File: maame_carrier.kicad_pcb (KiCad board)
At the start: 2 copper layers, 95 x 95 mm, 22 parts, among them J1 To Kakute H7 V1.5: full left 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, J10 FS-iA10B iBUS servo lead (S +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, J11 TF-Luna pin order 1-6 (CFG ti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, J12 Spare FC I2C (5 V supply, sha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, J13 Payload servo power (+ -); se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, J17 Kakute spare: T3 RSSI 3V3(FC)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, J3 VBAT tap from ESC battery pad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, J4 Micro BEC input leads (6-60 V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, J5 Micro BEC output leads (set t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, J6 Spare power: 5V_AUX G 5V_FC G, J7 Pi expansion: 3V3 logic ONLY, J8 TBS M10Q: order matches its p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, J9 SiK radio (UART4), U1 Raspberry Pi Zero W v1.1, com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

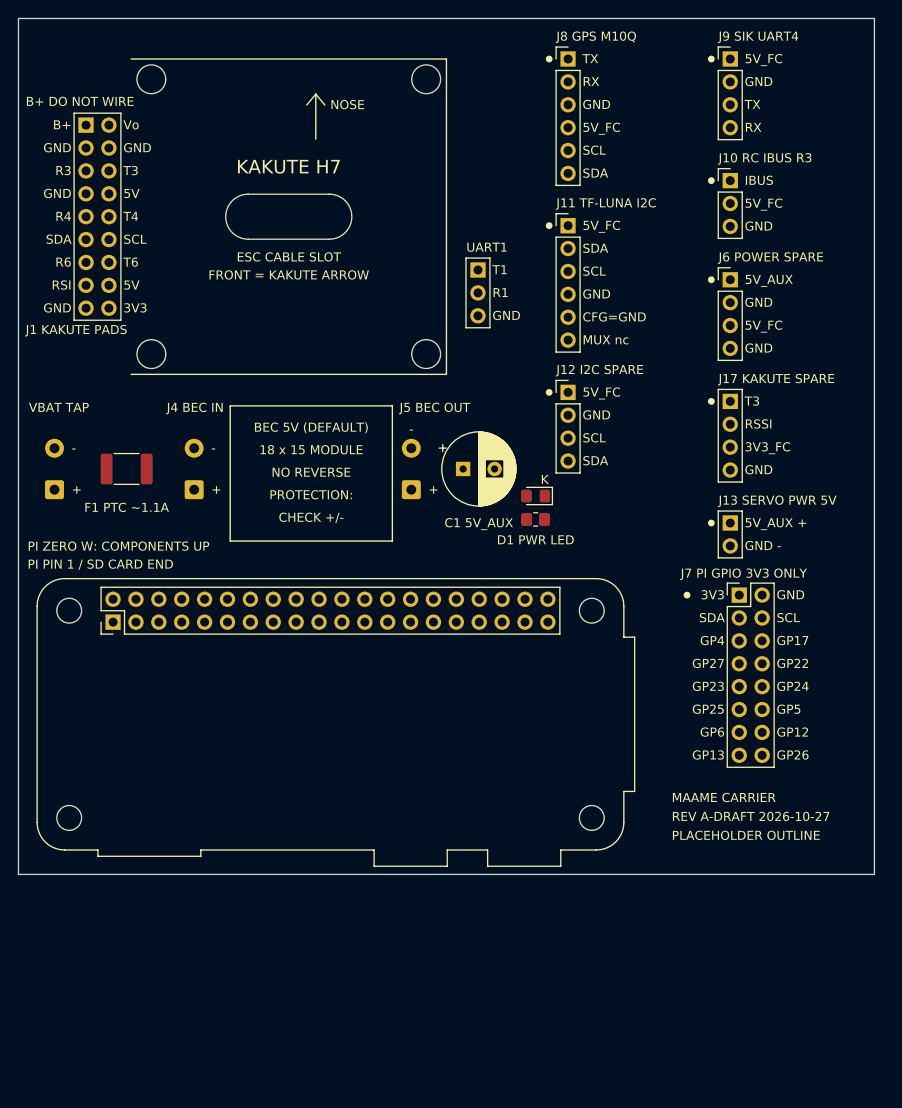
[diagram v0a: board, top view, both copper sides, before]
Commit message: J1 mirrors the Kakute's top (G 5V Vi CAM) and bottom (Z- 5V G LED) pad rows; J17 gains BUZ- and LED; J13 under J12; template and render refreshed
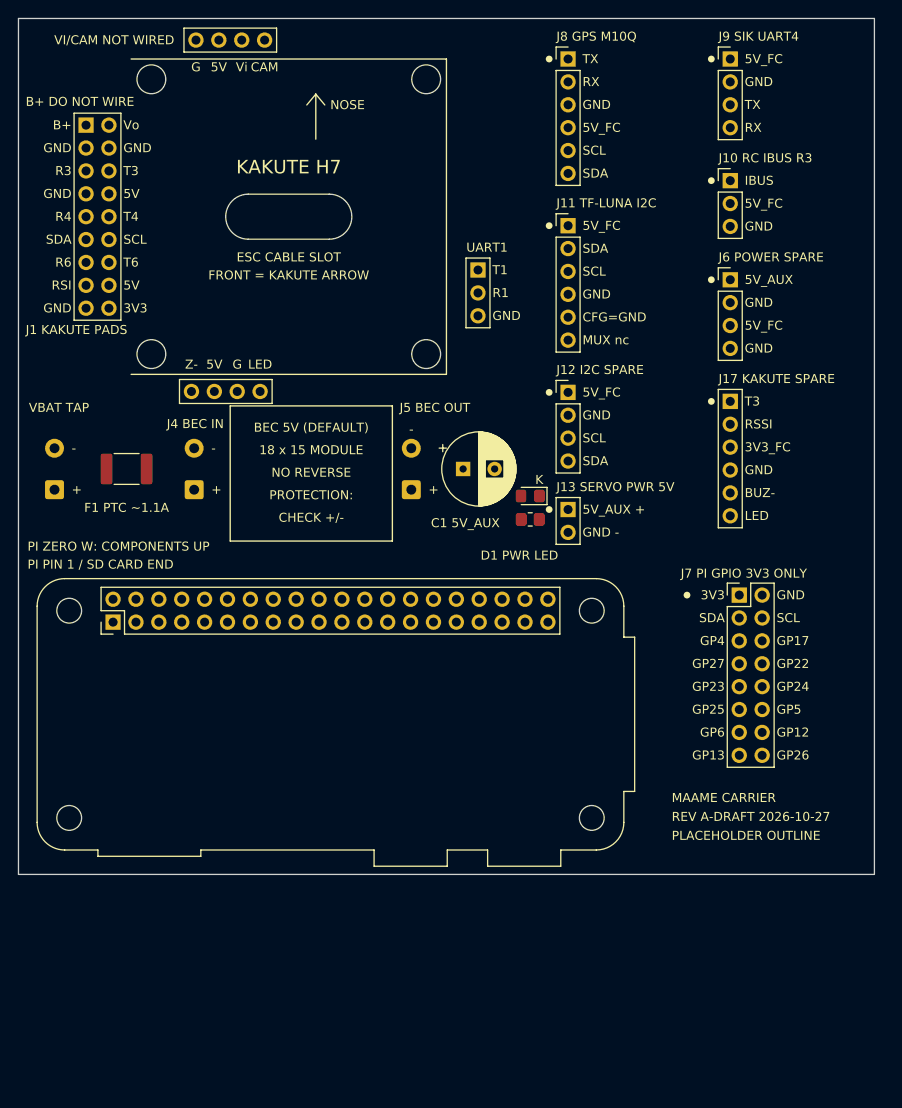
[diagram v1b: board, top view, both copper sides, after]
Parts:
- J1: value To Kakute H7 V1.5: full left pad strip 2x9 (B+ not wired) + JST T1 R1 G -> To Kakute H7 V1.5: left strip 2x9 (B+ not wired), top GND 5V Vi CAM, bottom Z- 5V GND LED, JST T1 R1 G
- J17: value Kakute spare: T3 RSSI 3V3(FC) G -> Kakute spare: T3 RSSI 3V3(FC) G BUZ- LED; footprint Connector_PinHeader_2.54mm:PinHeader_1x04_P2.54mm_Vertical -> Connector_PinHeader_2.54mm:PinHeader_1x06_P2.54mm_Vertical
- moved J13 18.1 mm to (61.0, 54.5)
- moved D1 0.60 mm to (56.8, 53.0)
- moved R1 0.60 mm to (56.8, 55.6)
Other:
- board text added: "BUZ-"
- board text added: "CAM"
- board text added: "G"
- board text added: "LED"
- board text added: "VI/CAM NOT WIRED"
- board text added: "Vi"
- board text added: "Z-"

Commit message: Frame mounting: 4x M2.5 (2.7 mm NPTH) on a 50 mm square centred on the Kakute; layout shifted, board 95x110; template updated
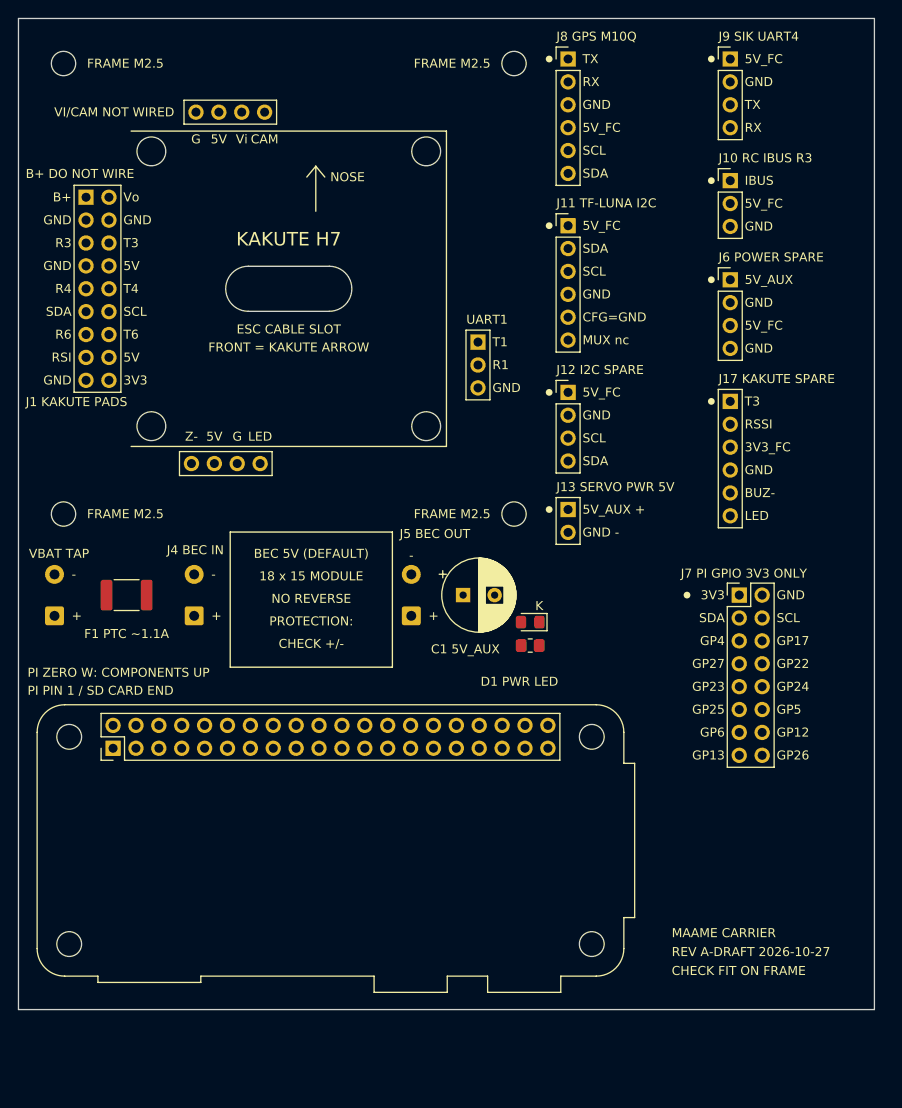
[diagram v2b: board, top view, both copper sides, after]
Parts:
- added H5: M2.5 frame mount (50 mm square), MountingHole:MountingHole_2.7mm_M2.5, F.Cu at (5.00, 5.00)
- added H6: M2.5 frame mount (50 mm square), MountingHole:MountingHole_2.7mm_M2.5, F.Cu at (55.0, 5.00)
- added H7: M2.5 frame mount (50 mm square), MountingHole:MountingHole_2.7mm_M2.5, F.Cu at (5.00, 55.0)
- added H8: M2.5 frame mount (50 mm square), MountingHole:MountingHole_2.7mm_M2.5, F.Cu at (55.0, 55.0)
- moved C1 14.0 mm to (49.4, 64.0)
- moved D1 14.0 mm to (56.8, 67.0)
- moved F1 14.0 mm to (12.0, 64.0)
- moved J3 14.0 mm to (4.00, 66.3)
- moved J4 14.0 mm to (19.5, 66.3)
- moved J5 14.0 mm to (43.6, 66.3)
- moved U1 14.0 mm to (10.5, 81.0)
- moved R1 14.0 mm to (56.8, 69.6)
- moved H1 8.00 mm to (14.8, 14.8)
- moved H2 8.00 mm to (45.2, 14.8)
- moved H3 8.00 mm to (14.8, 45.2)
- moved H4 8.00 mm to (45.2, 45.2)
- moved J1 8.00 mm to (7.50, 19.8)
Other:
- board size 95 x 95 mm -> 95 x 110 mm
- board text added: "CHECK FIT ON FRAME"
- board text added: "FRAME M2.5"
- board text removed: "PLACEHOLDER OUTLINE"

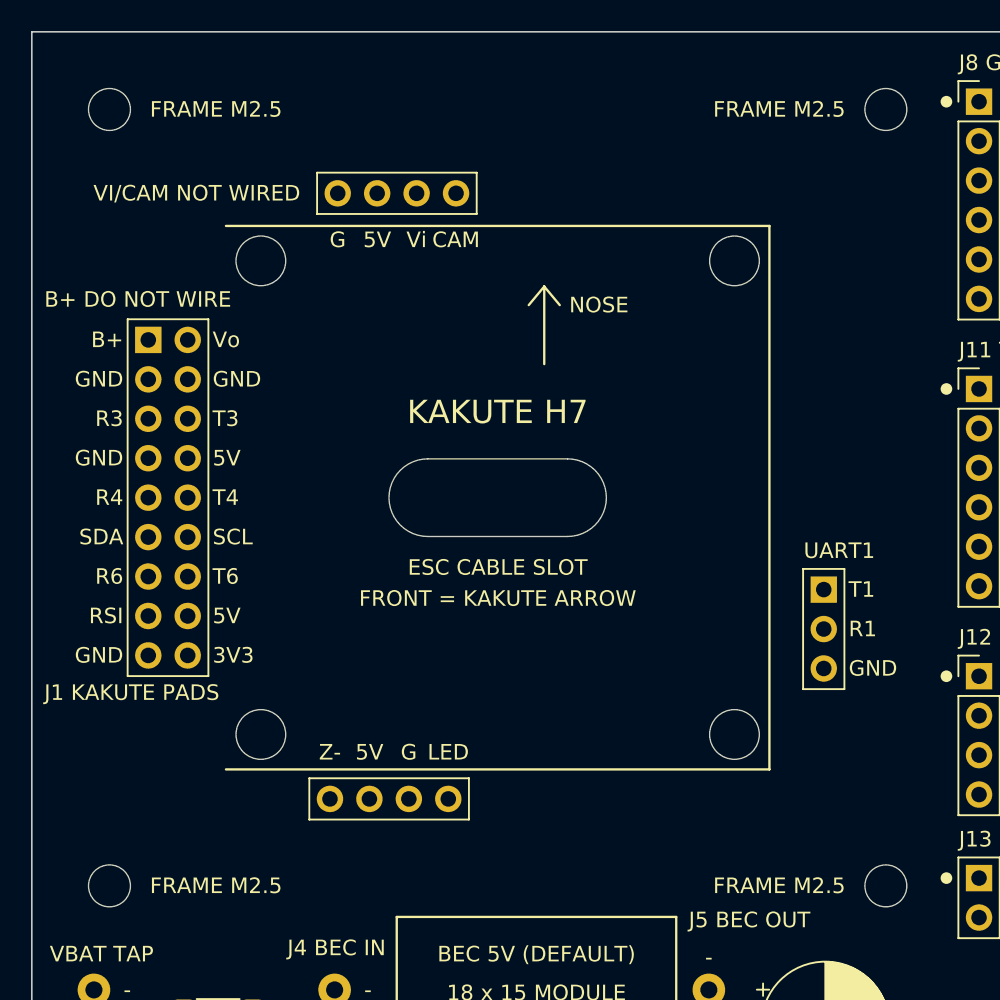
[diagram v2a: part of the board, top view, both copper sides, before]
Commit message: Frame holes measured from the pierced template: 48.3 mm square (was 50), M2.5 radial slots with +/-0.75 mm play
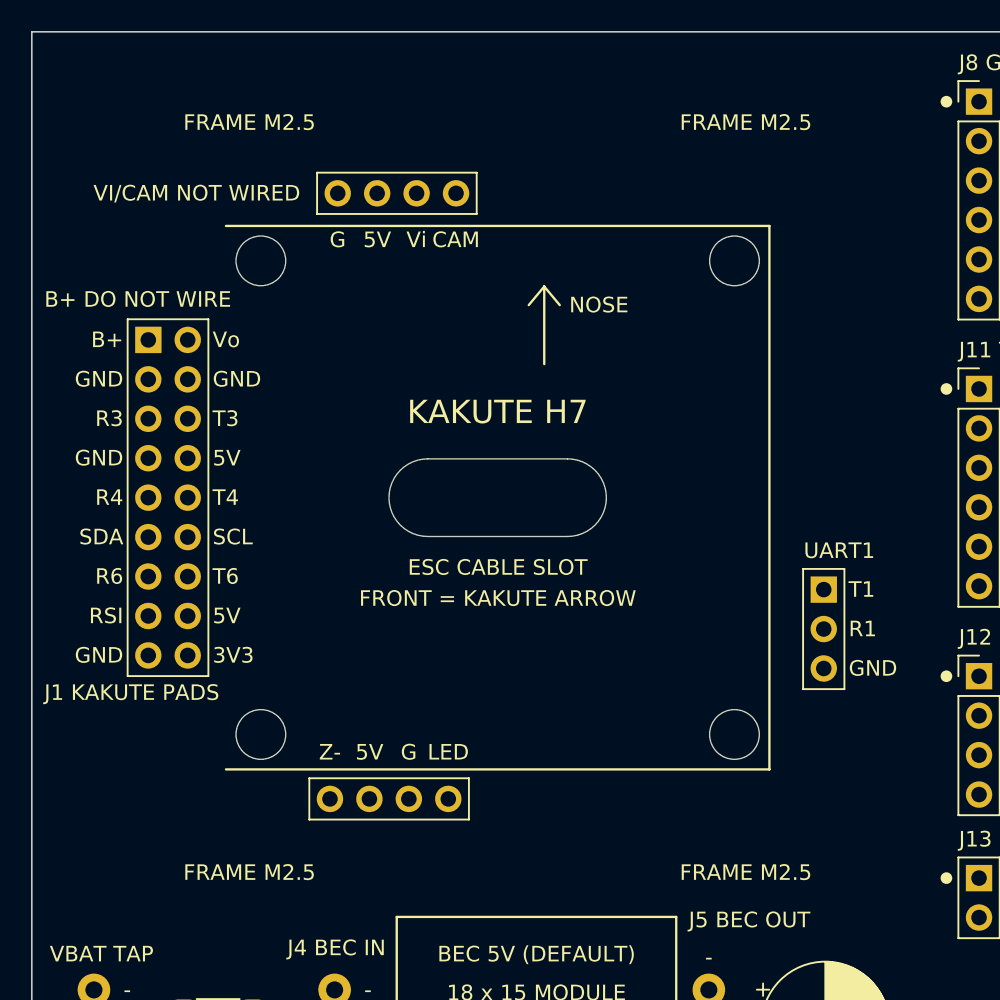
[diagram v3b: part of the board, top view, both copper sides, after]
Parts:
- H5, H6, H7, H8: value M2.5 frame mount (50 mm square) -> M2.5 frame mount, 48.3 mm square, radial slot
- moved H8 1.20 mm to (54.1, 54.1)
- moved H6 1.20 mm to (54.1, 5.85)
- moved H7 1.20 mm to (5.85, 54.1)
- moved H5 1.20 mm to (5.85, 5.85)
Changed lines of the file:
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@@
 	(footprint "MountingHole:MountingHole_2.7mm_M2.5"
 		(layer "F.Cu")
-		(at 5 5)
+		(at 5.85 5.85)
 		(descr "Mounting Hole 2.7mm, no annular, M2.5")
 		(tags "mounting hole 2.7mm no annular m2.5")
@@
 			)
 		)
-		(property "Value" "M2.5 frame mount (50 mm square)"
+		(property "Value" "M2.5 frame mount, 48.3 mm square, radial slot"
 			(at 0 3.7 0)
 			(layer "F.Fab")
@@
 		(fp_circle
 			(center 0 0)
-			(end 2.7 0)
+			(end 3.5 0)
 			(stroke
 				(width 0.15)
@@
 		(fp_circle
 			(center 0 0)
-			(end 2.95 0)
+			(end 3.7 0)
 			(stroke
 				(width 0.05)
@@
 			)
 		)
-		(pad "" np_thru_hole circle
-			(at 0 0)
-			(size 2.7 2.7)
-			(drill 2.7)
+		(pad "" np_thru_hole oval
+			(at 0 0 315)
+			(size 4.2 2.7)
+			(drill oval 4.2 2.7)
 			(layers "*.Cu" "*.Mask")
 		)
@@
 	(footprint "MountingHole:MountingHole_2.7mm_M2.5"
 		(layer "F.Cu")
-		(at 55 5)
+		(at 54.15 5.85)
 		(descr "Mounting Hole 2.7mm, no annular, M2.5")
 		(tags "mounting hole 2.7mm no annular m2.5")
@@
 			)
 		)
-		(property "Value" "M2.5 frame mount (50 mm square)"
+		(property "Value" "M2.5 frame mount, 48.3 mm square, radial slot"
 			(at 0 3.7 0)
 			(layer "F.Fab")
@@
 		(fp_circle
 			(center 0 0)
-			(end 2.7 0)
+			(end 3.5 0)
 			(stroke
 				(width 0.15)
@@
 		(fp_circle
 			(center 0 0)
-			(end 2.95 0)
+			(end 3.7 0)
 			(stroke
 				(width 0.05)
@@
 			)
 		)
-		(pad "" np_thru_hole circle
-			(at 0 0)
-			(size 2.7 2.7)
-			(drill 2.7)
+		(pad "" np_thru_hole oval
+			(at 0 0 45)
+			(size 4.2 2.7)
+			(drill oval 4.2 2.7)
 			(layers "*.Cu" "*.Mask")
 		)
@@
 	(footprint "MountingHole:MountingHole_2.7mm_M2.5"
 		(layer "F.Cu")
-		(at 5 55)
+		(at 5.85 54.15)
 		(descr "Mounting Hole 2.7mm, no annular, M2.5")
 		(tags "mounting hole 2.7mm no annular m2.5")
@@
 			)
 		)
-		(property "Value" "M2.5 frame mount (50 mm square)"
+		(property "Value" "M2.5 frame mount, 48.3 mm square, radial slot"
 			(at 0 3.7 0)
 			(layer "F.Fab")
@@
 		(fp_circle
 			(center 0 0)
-			(end 2.7 0)
+			(end 3.5 0)
 			(stroke
 				(width 0.15)
@@
 		(fp_circle
 			(center 0 0)
-			(end 2.95 0)
+			(end 3.7 0)
 			(stroke
 				(width 0.05)
@@
 			)
 		)
-		(pad "" np_thru_hole circle
-			(at 0 0)
-			(size 2.7 2.7)
-			(drill 2.7)
+		(pad "" np_thru_hole oval
+			(at 0 0 45)
+			(size 4.2 2.7)
+			(drill oval 4.2 2.7)
 			(layers "*.Cu" "*.Mask")
 		)
@@
 	(footprint "MountingHole:MountingHole_2.7mm_M2.5"
 		(layer "F.Cu")
-		(at 55 55)
+		(at 54.15 54.15)
 		(descr "Mounting Hole 2.7mm, no annular, M2.5")
 		(tags "mounting hole 2.7mm no annular m2.5")
@@
 			)
 		)
-		(property "Value" "M2.5 frame mount (50 mm square)"
+		(property "Value" "M2.5 frame mount, 48.3 mm square, radial slot"
 			(at 0 3.7 0)
 			(layer "F.Fab")
@@
 		(fp_circle
 			(center 0 0)
-			(end 2.7 0)
+			(end 3.5 0)
 			(stroke
 				(width 0.15)
@@
 		(fp_circle
 			(center 0 0)
-			(end 2.95 0)
+			(end 3.7 0)
 			(stroke
 				(width 0.05)
@@
 			)
 		)
-		(pad "" np_thru_hole circle
-			(at 0 0)
-			(size 2.7 2.7)
-			(drill 2.7)
+		(pad "" np_thru_hole oval
+			(at 0 0 315)
+			(size 4.2 2.7)
+			(drill oval 4.2 2.7)
 			(layers "*.Cu" "*.Mask")
 		)
@@
 	)
 	(gr_text "FRAME M2.5"
-		(at 7.6 5 0)
+		(at 9.75 5.85 0)
 		(layer "F.SilkS")
 		(effects
@@
 	)
 	(gr_text "FRAME M2.5"
-		(at 52.4 5 0)
+		(at 50.25 5.85 0)
 		(layer "F.SilkS")
 		(effects
@@
 	)
 	(gr_text "FRAME M2.5"
-		(at 7.6 55 0)
+		(at 9.75 54.15 0)
 		(layer "F.SilkS")
 		(effects
@@
 	)
 	(gr_text "FRAME M2.5"
-		(at 52.4 55 0)
+		(at 50.25 54.15 0)
 		(layer "F.SilkS")
 		(effects

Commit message: Frame holes to measured 48.5 mm square (M2.5 radial slots kept)
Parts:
- H5, H6, H7, H8: value M2.5 frame mount, 48.3 mm square, radial slot -> M2.5 frame mount, 48.5 mm square, radial slot
- moved H8 0.14 mm to (54.2, 54.2)
- moved H6 0.14 mm to (54.2, 5.75)
- moved H7 0.14 mm to (5.75, 54.2)
- moved H5 0.14 mm to (5.75, 5.75)
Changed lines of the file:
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@@
 	(footprint "MountingHole:MountingHole_2.7mm_M2.5"
 		(layer "F.Cu")
-		(at 5.85 5.85)
+		(at 5.75 5.75)
 		(descr "Mounting Hole 2.7mm, no annular, M2.5")
 		(tags "mounting hole 2.7mm no annular m2.5")
@@
 			)
 		)
-		(property "Value" "M2.5 frame mount, 48.3 mm square, radial slot"
+		(property "Value" "M2.5 frame mount, 48.5 mm square, radial slot"
 			(at 0 3.7 0)
 			(layer "F.Fab")
@@
 	(footprint "MountingHole:MountingHole_2.7mm_M2.5"
 		(layer "F.Cu")
-		(at 54.15 5.85)
+		(at 54.25 5.75)
 		(descr "Mounting Hole 2.7mm, no annular, M2.5")
 		(tags "mounting hole 2.7mm no annular m2.5")
@@
 			)
 		)
-		(property "Value" "M2.5 frame mount, 48.3 mm square, radial slot"
+		(property "Value" "M2.5 frame mount, 48.5 mm square, radial slot"
 			(at 0 3.7 0)
 			(layer "F.Fab")
@@
 	(footprint "MountingHole:MountingHole_2.7mm_M2.5"
 		(layer "F.Cu")
-		(at 5.85 54.15)
+		(at 5.75 54.25)
 		(descr "Mounting Hole 2.7mm, no annular, M2.5")
 		(tags "mounting hole 2.7mm no annular m2.5")
@@
 			)
 		)
-		(property "Value" "M2.5 frame mount, 48.3 mm square, radial slot"
+		(property "Value" "M2.5 frame mount, 48.5 mm square, radial slot"
 			(at 0 3.7 0)
 			(layer "F.Fab")
@@
 	(footprint "MountingHole:MountingHole_2.7mm_M2.5"
 		(layer "F.Cu")
-		(at 54.15 54.15)
+		(at 54.25 54.25)
 		(descr "Mounting Hole 2.7mm, no annular, M2.5")
 		(tags "mounting hole 2.7mm no annular m2.5")
@@
 			)
 		)
-		(property "Value" "M2.5 frame mount, 48.3 mm square, radial slot"
+		(property "Value" "M2.5 frame mount, 48.5 mm square, radial slot"
 			(at 0 3.7 0)
 			(layer "F.Fab")
@@
 	)
 	(gr_text "FRAME M2.5"
-		(at 9.75 5.85 0)
+		(at 9.65 5.75 0)
 		(layer "F.SilkS")
 		(effects
@@
 	)
 	(gr_text "FRAME M2.5"
-		(at 50.25 5.85 0)
+		(at 50.35 5.75 0)
 		(layer "F.SilkS")
 		(effects
@@
 	)
 	(gr_text "FRAME M2.5"
-		(at 9.75 54.15 0)
+		(at 9.65 54.25 0)
 		(layer "F.SilkS")
 		(effects
@@
 	)
 	(gr_text "FRAME M2.5"
-		(at 50.25 54.15 0)
+		(at 50.35 54.25 0)
 		(layer "F.SilkS")
 		(effects

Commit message: Silkscreen: standoff >= 10 mm and lead-trim note
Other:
- board text added: "STANDOFFS M2.5 >= 10MM"
- board text added: "TRIM LEADS <= 1.5MM"
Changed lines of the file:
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@@
+		)
+	)
+	(gr_text "STANDOFFS M2.5 >= 10MM"
+		(at 72.5 96.9 0)
+		(layer "F.SilkS")
+		(effects
+			(font
+				(size 1 1)
+				(thickness 0.15)
+			)
+			(justify left)
+		)
+	)
+	(gr_text "TRIM LEADS <= 1.5MM"
+		(at 72.5 99 0)
+		(layer "F.SilkS")
+		(effects
+			(font
+				(size 1 1)
+				(thickness 0.15)
+			)
+			(justify left)
 		)
 	)
